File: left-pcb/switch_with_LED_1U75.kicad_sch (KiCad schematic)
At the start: 3 parts, among them SW5 SW_SPST

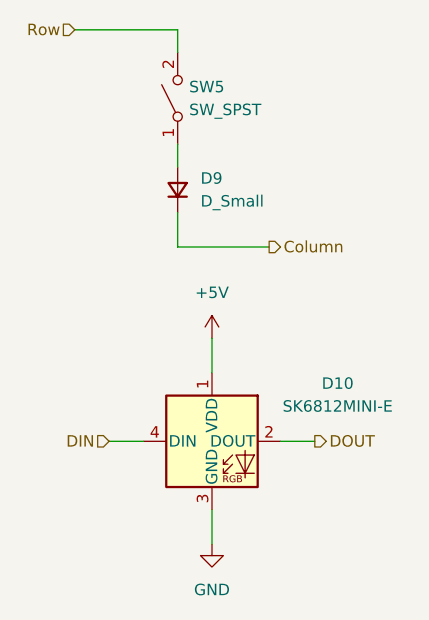
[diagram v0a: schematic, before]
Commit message: Initial modifications to reduce fab cost and add caps
Removing 1 row and column of keys, and majorly changing layout

Routing still in progress
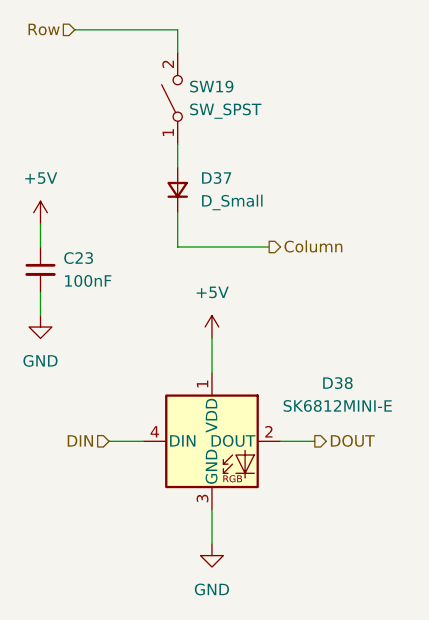
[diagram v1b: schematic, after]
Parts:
- removed D10: SK6812MINI-E, SW-Adafruit:LED_SK6812MINI-E_REVERSE_MOUNT_3.2x2.8mm_P1.09mm, symbol SW-Adafruit:SK6812MINI-E
- removed D9: D_Small, Diode_SMD:D_SOD-123, symbol Device:D_Small
- removed SW5: SW_SPST, PCM_Switch_Keyboard_Hotswap_Kailh:SW_Hotswap_Kailh_MX_1.75u, symbol Switch:SW_SPST
- added C23: 100nF, Capacitor_SMD:C_1206_3216Metric_Pad1.33x1.80mm_HandSolder, symbol Device:C_Small
- added D37: D_Small, Diode_SMD:D_SOD-123, symbol Device:D_Small
- added D38: SK6812MINI-E, SW-Adafruit:LED_SK6812MINI-E_REVERSE_MOUNT_3.2x2.8mm_P1.09mm, symbol SW-Adafruit:SK6812MINI-E
- added SW19: SW_SPST, PCM_Switch_Keyboard_Hotswap_Kailh:SW_Hotswap_Kailh_MX_1.75u, symbol Switch:SW_SPST
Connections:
- net +5V: now also C23.1, D38.1 (VDD)
- net Column: now also D37.1 (K)
- net DIN: now also D38.4 (DIN)
- net DOUT: now also D38.2 (DOUT)
- net GND: now also C23.2, D38.3 (GND)
- net Row: now also SW19.2 (B)
- new net: D37.2 (A), SW19.1 (A)

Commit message: Caps, shrunk board, added mounting holes
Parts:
- C23: footprint Capacitor_SMD:C_1206_3216Metric_Pad1.33x1.80mm_HandSolder -> Capacitor_SMD:C_0805_2012Metric_Pad1.18x1.45mm_HandSolder
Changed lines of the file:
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@@
 			)
 		)
-		(property "Footprint" "Capacitor_SMD:C_1206_3216Metric_Pad1.33x1.80mm_HandSolder"
+		(property "Footprint" "Capacitor_SMD:C_0805_2012Metric_Pad1.18x1.45mm_HandSolder"
 			(at 105.41 113.03 0)
 			(effects

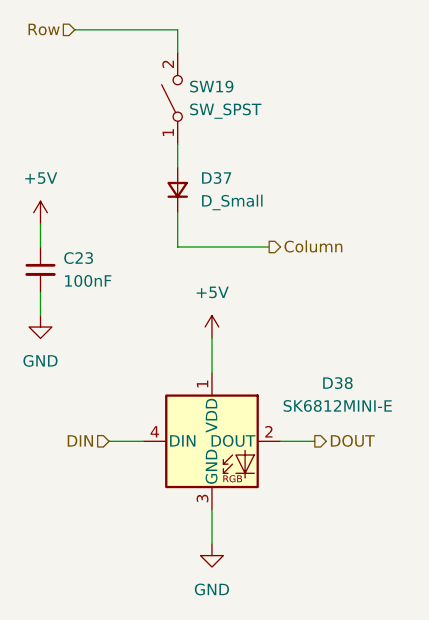
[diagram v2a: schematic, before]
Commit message: Adding values to Diodes and adding stabilizers to 2U switches
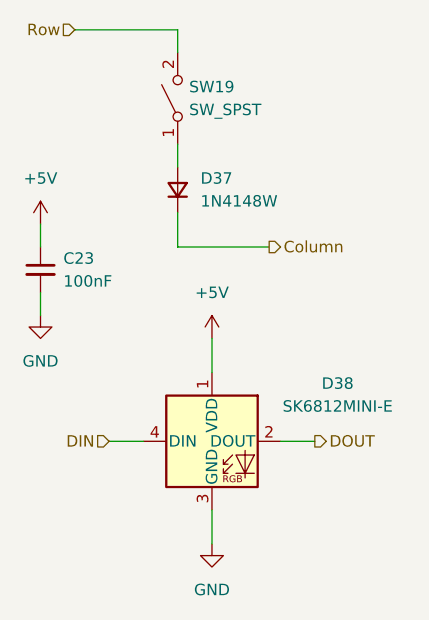
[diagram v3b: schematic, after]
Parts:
- D37: value D_Small -> 1N4148W
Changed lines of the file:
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@@
 			)
 		)
-		(property "Value" "D_Small"
+		(property "Value" "1N4148W"
 			(at 123.19 105.4099 90)
 			(effects

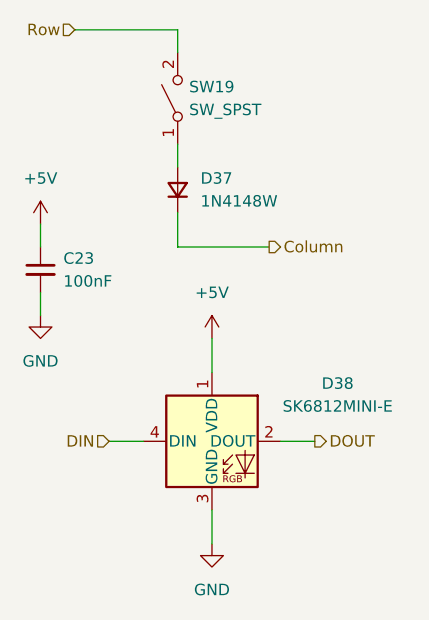
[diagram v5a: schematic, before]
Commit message: adding mounting hole in center for additional support, and cleaning up tracks/zones
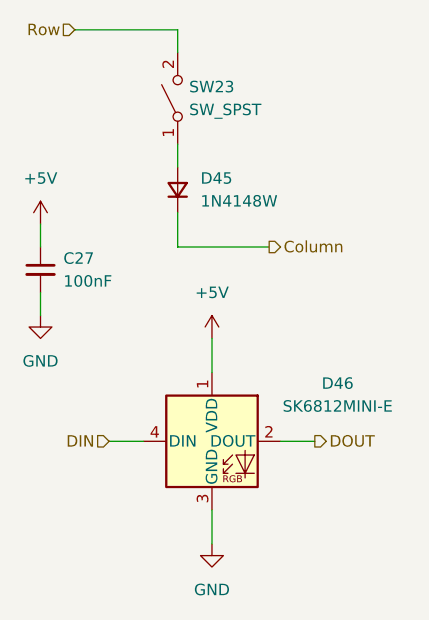
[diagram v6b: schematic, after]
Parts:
- renumbered C23 to C27, D37 to D45, D38 to D46, SW19 to SW23
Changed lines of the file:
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@@
+	(wire
+		(pts
+			(xy 124.46 120.65) (xy 124.46 124.46)
+		)
+		(stroke
+			(width 0)
+			(type default)
+		)
+	)
+	(wire
+		(pts
+			(xy 109.22 86.36) (xy 120.65 86.36)
+		)
+		(stroke
+			(width 0)
+			(type default)
+		)
+	)
 	(wire
 		(pts
@@
 	(wire
 		(pts
+			(xy 113.03 132.08) (xy 116.84 132.08)
+		)
+		(stroke
+			(width 0)
+			(type default)
+		)
+	)
+	(wire
+		(pts
+			(xy 132.08 132.08) (xy 135.89 132.08)
+		)
+		(stroke
+			(width 0)
+			(type default)
+		)
+	)
+	(wire
+		(pts
 			(xy 120.65 110.49) (xy 130.81 110.49)
 		)
@@
 	(wire
 		(pts
-			(xy 132.08 132.08) (xy 135.89 132.08)
-		)
-		(stroke
-			(width 0)
-			(type default)
-		)
-	)
-	(wire
-		(pts
-			(xy 109.22 86.36) (xy 120.65 86.36)
-		)
-		(stroke
-			(width 0)
-			(type default)
-		)
-	)
-	(wire
-		(pts
-			(xy 113.03 132.08) (xy 116.84 132.08)
-		)
-		(stroke
-			(width 0)
-			(type default)
-		)
-	)
-	(wire
-		(pts
 			(xy 124.46 139.7) (xy 124.46 143.51)
-		)
-		(stroke
-			(width 0)
-			(type default)
-		)
-	)
-	(wire
-		(pts
-			(xy 124.46 120.65) (xy 124.46 124.46)
 		)
 		(stroke
@@
 		(dnp no)
 		(fields_autoplaced yes)
-		(property "Reference" "D37"
+		(property "Reference" "D45"
 			(at 123.19 102.8699 90)
 			(show_name no)
@@
 			(project "row_staggered_split_keyboard_left_side"
 				(path "/cf145565-22e2-4e5a-8a27-915862c57a1b/458a0dcf-17de-4473-ba10-e24c951ff17a"
-					(reference "D37")
+					(reference "D45")
 					(unit 1)
 				)
@@
 		(dnp no)
 		(fields_autoplaced yes)
-		(property "Reference" "SW19"
+		(property "Reference" "SW23"
 			(at 121.92 92.7099 90)
 			(show_name no)
@@
 			(project "row_staggered_split_keyboard_left_side"
 				(path "/cf145565-22e2-4e5a-8a27-915862c57a1b/458a0dcf-17de-4473-ba10-e24c951ff17a"
-					(reference "SW19")
+					(reference "SW23")
 					(unit 1)
 				)
@@
 		(dnp no)
 		(fields_autoplaced yes)
-		(property "Reference" "D38"
+		(property "Reference" "D46"
 			(at 138.43 125.6598 0)
 			(show_name no)
@@
 			(project "row_staggered_split_keyboard_left_side"
 				(path "/cf145565-22e2-4e5a-8a27-915862c57a1b/458a0dcf-17de-4473-ba10-e24c951ff17a"
-					(reference "D38")
+					(reference "D46")
 					(unit 1)
 				)
@@
 		(dnp no)
 		(fields_autoplaced yes)
-		(property "Reference" "#PWR092"
+		(property "Reference" "#PWR0108"
 			(at 124.46 149.86 0)
 			(hide yes)
@@
 			(project "row_staggered_split_keyboard_left_side"
 				(path "/cf145565-22e2-4e5a-8a27-915862c57a1b/458a0dcf-17de-4473-ba10-e24c951ff17a"
-					(reference "#PWR092")
+					(reference "#PWR0108")
 					(unit 1)
 				)
@@
 		(dnp no)
 		(fields_autoplaced yes)
-		(property "Reference" "C23"
+		(property "Reference" "C27"
 			(at 107.95 111.7662 0)
 			(show_name no)
@@
 			(project "row_staggered_split_keyboard_left_side"
 				(path "/cf145565-22e2-4e5a-8a27-915862c57a1b/458a0dcf-17de-4473-ba10-e24c951ff17a"
-					(reference "C23")
+					(reference "C27")
 					(unit 1)
 				)
@@
 		(dnp no)
 		(fields_autoplaced yes)
-		(property "Reference" "#PWR089"
+		(property "Reference" "#PWR0105"
 			(at 105.41 111.76 0)
 			(hide yes)
@@
 			(project "row_staggered_split_keyboard_left_side"
 				(path "/cf145565-22e2-4e5a-8a27-915862c57a1b/458a0dcf-17de-4473-ba10-e24c951ff17a"
-					(reference "#PWR089")
+					(reference "#PWR0105")
 					(unit 1)
 				)
@@
 		(dnp no)
 		(fields_autoplaced yes)
-		(property "Reference" "#PWR090"
+		(property "Reference" "#PWR0106"
 			(at 105.41 124.46 0)
 			(hide yes)
@@
 			(project "row_staggered_split_keyboard_left_side"
 				(path "/cf145565-22e2-4e5a-8a27-915862c57a1b/458a0dcf-17de-4473-ba10-e24c951ff17a"
-					(reference "#PWR090")
+					(reference "#PWR0106")
 					(unit 1)
 				)
@@
 		(dnp no)
 		(fields_autoplaced yes)
-		(property "Reference" "#PWR091"
+		(property "Reference" "#PWR0107"
 			(at 124.46 124.46 0)
 			(hide yes)
@@
 			(project "row_staggered_split_keyboard_left_side"
 				(path "/cf145565-22e2-4e5a-8a27-915862c57a1b/458a0dcf-17de-4473-ba10-e24c951ff17a"
-					(reference "#PWR091")
+					(reference "#PWR0107")
 					(unit 1)
 				)

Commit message: Boards were ordered
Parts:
- SW23: symbol Switch:SW_SPST -> SW-gElectroMech:SPST_MOM
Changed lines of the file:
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@@
 	)
 	(symbol
-		(lib_id "Switch:SW_SPST")
+		(lib_id "SW-gElectroMech:SPST_MOM")
 		(at 120.65 93.98 90)
 		(unit 1)
@@
 		)
 		(property "Datasheet" ""
-			(at 120.65 93.98 0)
+			(at 115.57 93.98 0)
 			(hide yes)
 			(show_name no)
@@
 			)
 		)
-		(property "Description" "Single Pole Single Throw (SPST) switch"
+		(property "Description" "Push button switch, generic, two pins"
 			(at 120.65 93.98 0)
 			(hide yes)
